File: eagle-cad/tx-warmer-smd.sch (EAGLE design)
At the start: 27 parts, among them Q1 MOSFET-NCHANNELFDS6630A, U2 V_REG_LDOSMD

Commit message: Minor updates to SMD-version
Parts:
- Q1: value MOSFET-NCHANNELFDS6630A -> IR F8721
- U2: value V_REG_LDOSMD -> MCP1804T
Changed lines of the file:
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@@
 <part name="R7" library="SparkFun-Resistors" deviceset="RESISTOR" device="0805-RES" value="100k"/>
 <part name="GND8" library="SparkFun-Aesthetics" deviceset="GND" device=""/>
-<part name="Q1" library="SparkFun-DiscreteSemi" deviceset="MOSFET-NCHANNEL" device="FDS6630A"/>
+<part name="Q1" library="SparkFun-DiscreteSemi" deviceset="MOSFET-NCHANNEL" device="FDS6630A" value="IR F8721"/>
 <part name="B-" library="SparkFun-Connectors" deviceset="M01" device="PTH_2MM"/>
 <part name="H-" library="SparkFun-Connectors" deviceset="M01" device="PTH_2MM"/>
@@
 <part name="C5" library="SparkFun-Capacitors" deviceset="CAP" device="0805" value="0.1uF"/>
 <part name="GND4" library="SparkFun-Aesthetics" deviceset="GND" device=""/>
-<part name="U2" library="SparkFun-PowerIC" deviceset="V_REG_LDO" device="SMD"/>
+<part name="U2" library="SparkFun-PowerIC" deviceset="V_REG_LDO" device="SMD" value="MCP1804T"/>
 <part name="S1" library="SparkFun-Electromechanical" deviceset="TAC_SWITCH" device="SMD"/>
 <part name="TP1" library="SparkFun-Passives" deviceset="TEST-POINT" device="3"/>

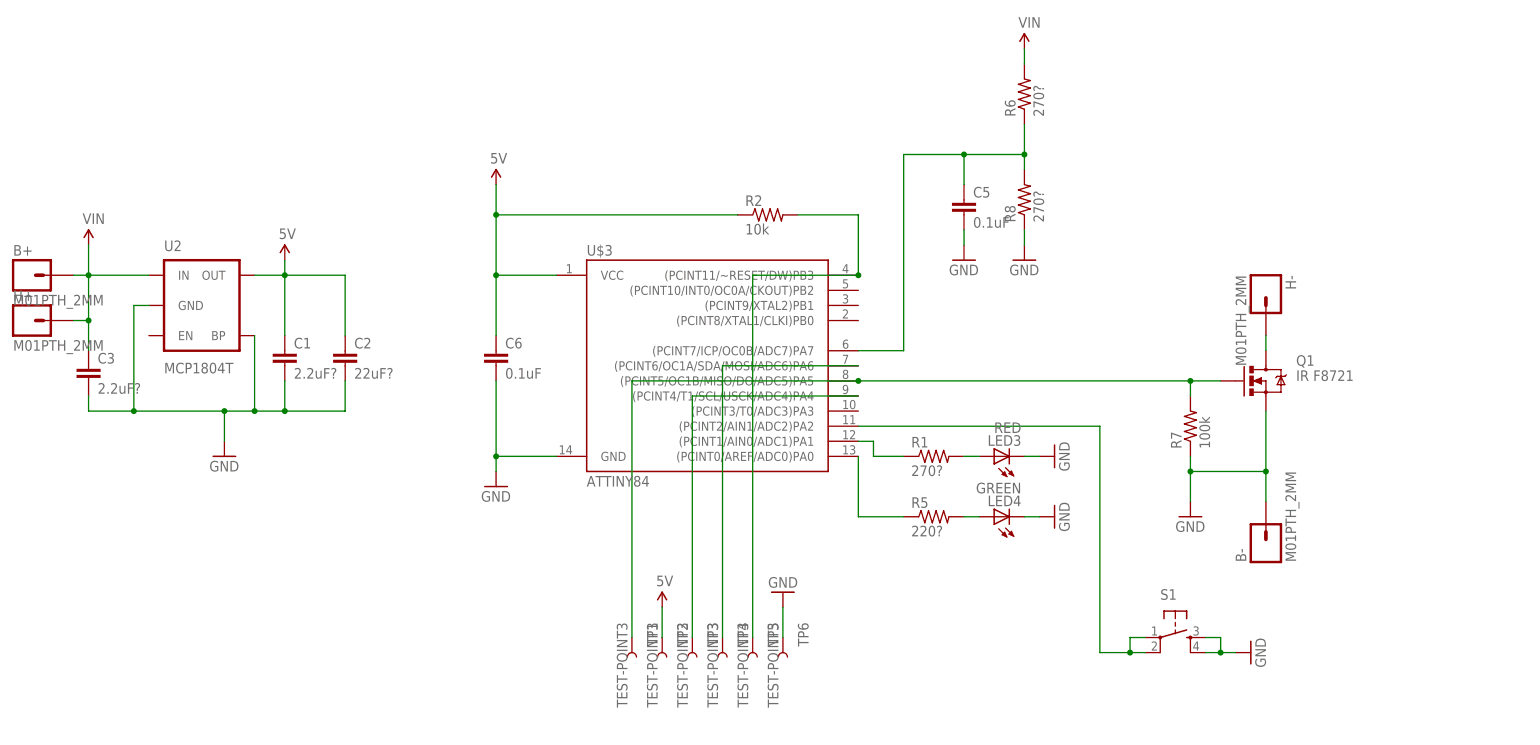
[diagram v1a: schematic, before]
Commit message: Fixed ldo shutdown-pin and checked values for res/caps
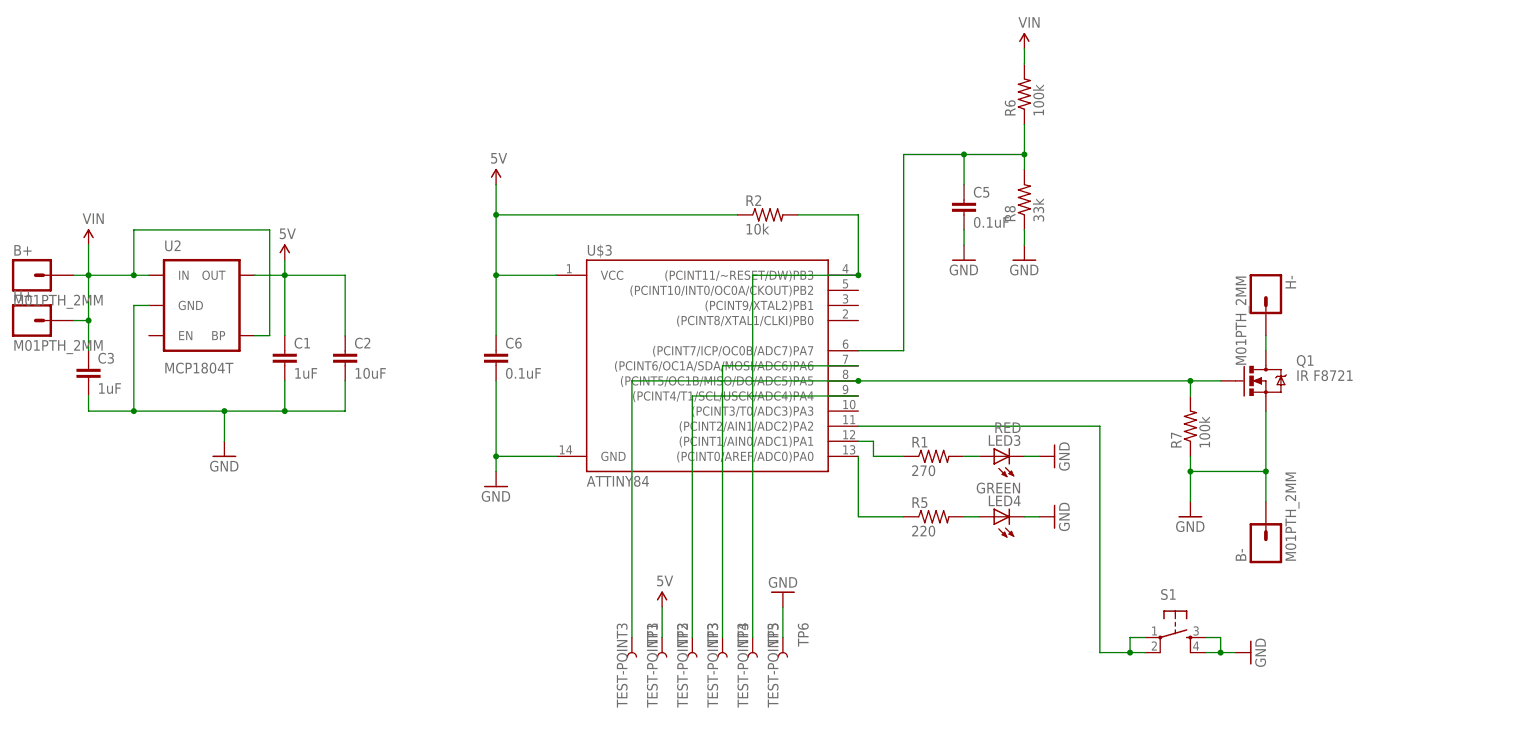
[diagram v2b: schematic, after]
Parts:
- C1, C3: value 2.2uF? -> 1uF
- C2: value 22uF? -> 10uF
- R1: value 270? -> 270
- R5: value 220? -> 220
- R6: value 270? -> 100k
- R8: value 270? -> 33k
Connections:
- net GND: no longer U2.BP
- net VIN: now also U2.BP
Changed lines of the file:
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@@
 <part name="GND10" library="SparkFun-Aesthetics" deviceset="GND" device=""/>
 <part name="R2" library="SparkFun-Resistors" deviceset="RESISTOR" device="0805-RES" value="10k"/>
-<part name="R1" library="SparkFun-Resistors" deviceset="RESISTOR" device="0805-RES" value="270?"/>
-<part name="R5" library="SparkFun-Resistors" deviceset="RESISTOR" device="0805-RES" value="220?"/>
+<part name="R1" library="SparkFun-Resistors" deviceset="RESISTOR" device="0805-RES" value="270"/>
+<part name="R5" library="SparkFun-Resistors" deviceset="RESISTOR" device="0805-RES" value="220"/>
 <part name="LED3" library="SparkFun-LED" deviceset="LED" device="1206" value="RED"/>
 <part name="LED4" library="SparkFun-LED" deviceset="LED" device="1206" value="GREEN"/>
@@
 <part name="H-" library="SparkFun-Connectors" deviceset="M01" device="PTH_2MM"/>
 <part name="GND2" library="SparkFun-Aesthetics" deviceset="GND" device=""/>
-<part name="C3" library="SparkFun-Capacitors" deviceset="CAP" device="0805" value="2.2uF?"/>
+<part name="C3" library="SparkFun-Capacitors" deviceset="CAP" device="0805" value="1uF"/>
 <part name="U$2" library="SparkFun-Aesthetics" deviceset="5V" device=""/>
-<part name="C1" library="SparkFun-Capacitors" deviceset="CAP" device="0805" value="2.2uF?"/>
+<part name="C1" library="SparkFun-Capacitors" deviceset="CAP" device="0805" value="1uF"/>
 <part name="SUPPLY1" library="SparkFun-Aesthetics" deviceset="VIN" device=""/>
-<part name="C2" library="SparkFun-Capacitors" deviceset="CAP" device="0805" value="22uF?"/>
+<part name="C2" library="SparkFun-Capacitors" deviceset="CAP" device="0805" value="10uF"/>
 <part name="SUPPLY2" library="SparkFun-Aesthetics" deviceset="VIN" device=""/>
-<part name="R6" library="SparkFun-Resistors" deviceset="RESISTOR" device="0805-RES" value="270?"/>
-<part name="R8" library="SparkFun-Resistors" deviceset="RESISTOR" device="0805-RES" value="270?"/>
+<part name="R6" library="SparkFun-Resistors" deviceset="RESISTOR" device="0805-RES" value="100k"/>
+<part name="R8" library="SparkFun-Resistors" deviceset="RESISTOR" device="0805-RES" value="33k"/>
 <part name="GND1" library="SparkFun-Aesthetics" deviceset="GND" device=""/>
 <part name="C5" library="SparkFun-Capacitors" deviceset="CAP" device="0805" value="0.1uF"/>
@@
 <pinref part="C1" gate="G$1" pin="2"/>
 <wire x1="12.7" y1="43.18" x2="27.94" y2="43.18" width="0.1524" layer="91"/>
-<wire x1="27.94" y1="43.18" x2="33.02" y2="43.18" width="0.1524" layer="91"/>
-<wire x1="33.02" y1="43.18" x2="38.1" y2="43.18" width="0.1524" layer="91"/>
+<wire x1="27.94" y1="43.18" x2="38.1" y2="43.18" width="0.1524" layer="91"/>
 <wire x1="38.1" y1="43.18" x2="38.1" y2="48.26" width="0.1524" layer="91"/>
 <pinref part="C2" gate="G$1" pin="2"/>
@@
 <wire x1="48.26" y1="43.18" x2="48.26" y2="48.26" width="0.1524" layer="91"/>
 <junction x="38.1" y="43.18"/>
-<pinref part="U2" gate="G$1" pin="BP"/>
-<wire x1="33.02" y1="55.88" x2="33.02" y2="43.18" width="0.1524" layer="91"/>
-<junction x="33.02" y="43.18"/>
 <pinref part="U2" gate="G$1" pin="GND"/>
 <wire x1="15.24" y1="60.96" x2="12.7" y2="60.96" width="0.1524" layer="91"/>
@@
 <junction x="5.08" y="66.04"/>
 <pinref part="U2" gate="G$1" pin="IN"/>
-<wire x1="15.24" y1="66.04" x2="5.08" y2="66.04" width="0.1524" layer="91"/>
-</segment>
-<segment>
+<wire x1="15.24" y1="66.04" x2="12.7" y2="66.04" width="0.1524" layer="91"/>
+<pinref part="U2" gate="G$1" pin="BP"/>
+<wire x1="12.7" y1="66.04" x2="5.08" y2="66.04" width="0.1524" layer="91"/>
+<wire x1="33.02" y1="55.88" x2="35.56" y2="55.88" width="0.1524" layer="91"/>
+<wire x1="35.56" y1="55.88" x2="35.56" y2="73.66" width="0.1524" layer="91"/>
+<wire x1="35.56" y1="73.66" x2="12.7" y2="73.66" width="0.1524" layer="91"/>
+<wire x1="12.7" y1="73.66" x2="12.7" y2="66.04" width="0.1524" layer="91"/>
+<junction x="12.7" y="66.04"/>
+</segment>
+<segment>
